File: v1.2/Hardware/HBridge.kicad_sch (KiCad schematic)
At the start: 54 parts, among them J10 DG25C-B-04P-13-00AH, J3 Screw_Terminal_01x03, J9 DG25C-B-04P-13-00AH, Q1 IXGH48N60C3D1, Q2 IXGH48N60C3D1, Q23 BC817, Q24 BC817, U8 HCPL-3120, U9 HCPL-3120

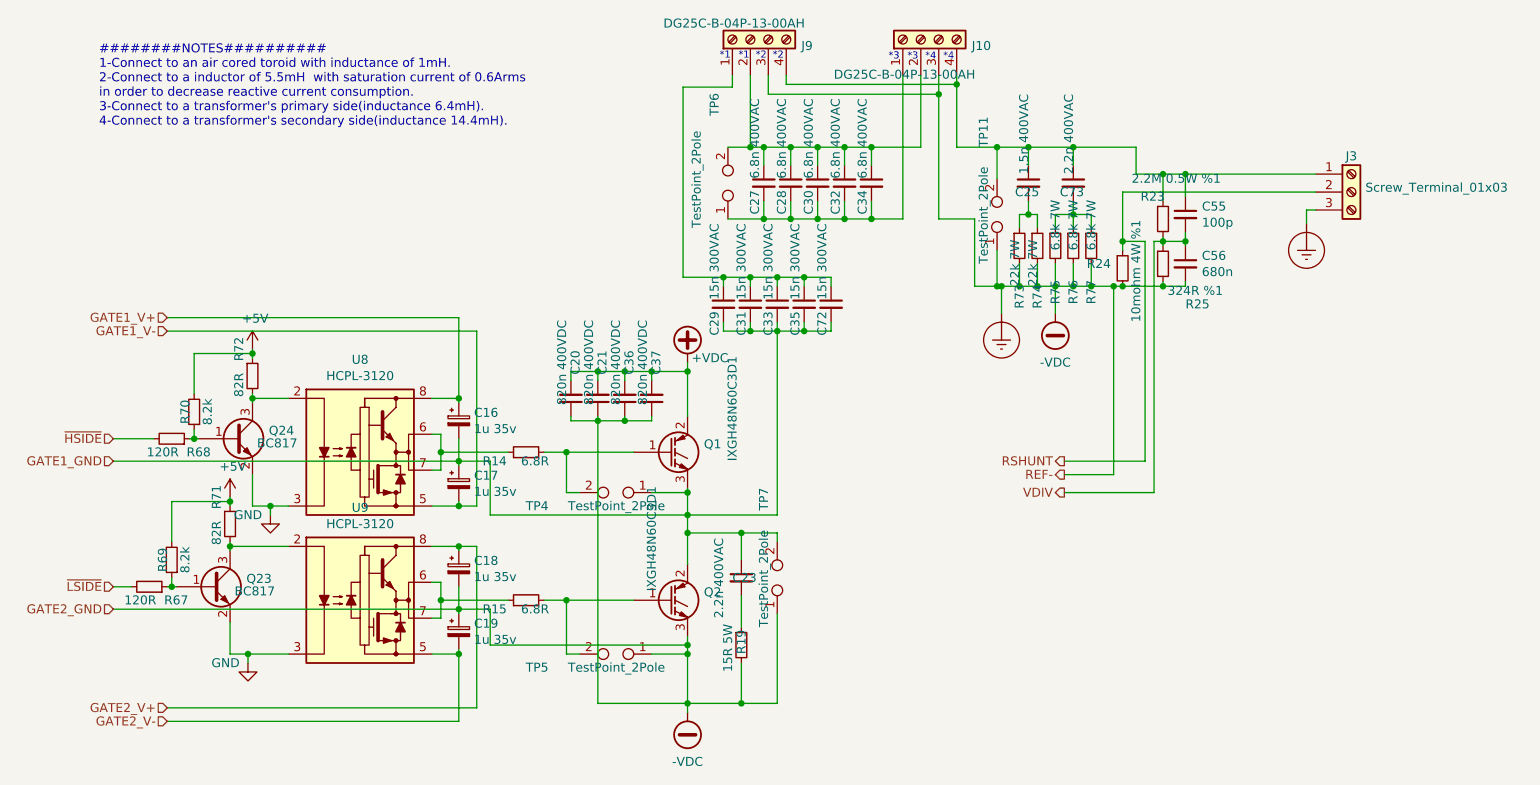
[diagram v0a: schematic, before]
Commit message: Addition of firmware to v1.2(not tested)
+Addition of power tracking(with duty cycle control).
+Addition of resonance freq tracking(via proprietary algorithm relied on active and reactive power measurements)
+Quality factor monitoring
+Power boost when loaded(idle and loaded modes)
+Much better frequency resolution(less than 1Hz)
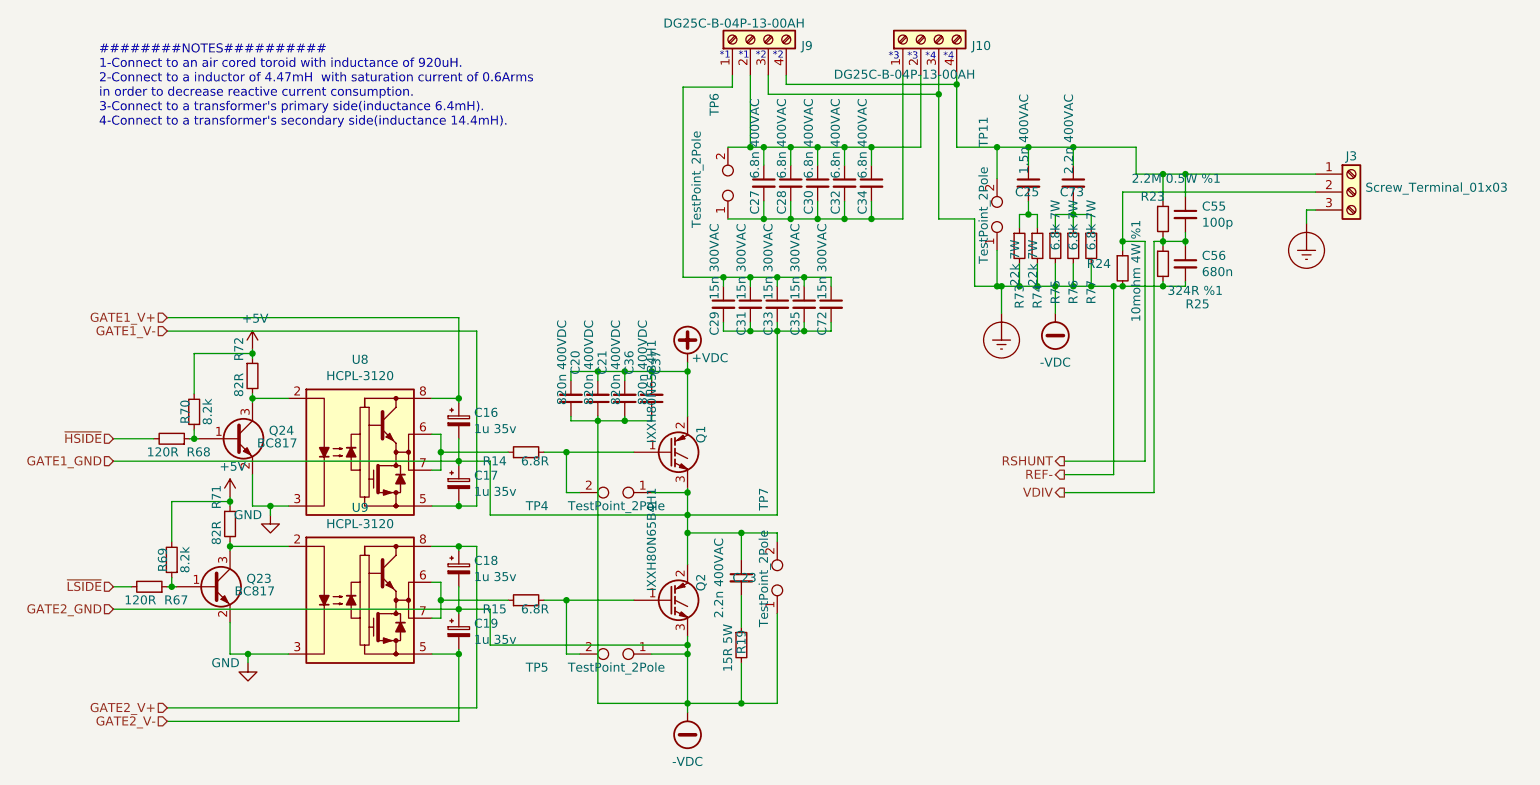
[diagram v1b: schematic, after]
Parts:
- Q1, Q2: value IXGH48N60C3D1 -> IXXH80N65B4H1; Link https://www.ozdisan.com/power-semiconductors/igbts/discrete-igbts/IXGH48N60C3D1 -> https://www.ozdisan.com/power-semiconductors/igbts/discrete-igbts/IXXH80N65B4H1; Price 25.41445TL -> 31.80527TL
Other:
- note added: "########NOTES########## 1-Connect to an air cored toroid with inductance of 920uH. 2-Connect to a inductor of 4.47mH with saturation current of 0.6Arms in order to decrease reactive current consumption. 3-Connect to a transformer's primary side(inductance 6.4mH). 4-Connect to a transformer's secondary side(inductance 14.4mH)."
- note removed: "########NOTES########## 1-Connect to an air cored toroid with inductance of 1mH. 2-Connect to a inductor of 5.5mH with saturation current of 0.6Arms in order to decrease reactive current consumption. 3-Connect to a transformer's primary side(inductance 6.4mH). 4-Connect to a transformer's secondary side(inductance 14.4mH)."

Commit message: Start of rs485 communication interface development.
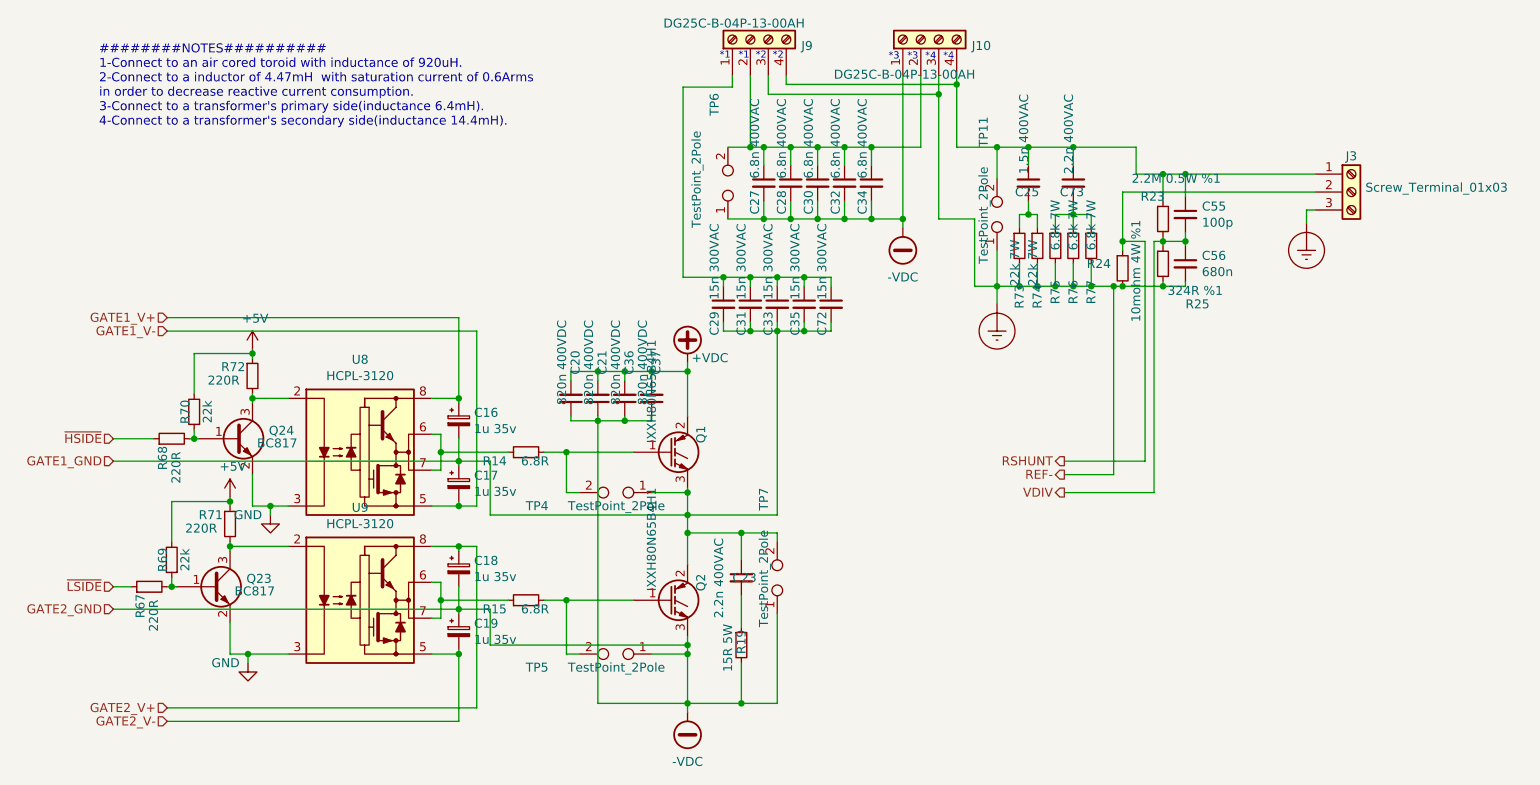
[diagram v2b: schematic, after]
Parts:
- R67, R68: value 120R -> 220R; Link https://ozdisan.com/passive-components/resistors/smt-smd-and-chip-resistors/0805S8J0121T5E -> https://ozdisan.com/passive-components/resistors/smt-smd-and-chip-resistors/0805S8J0221T5E; Price 0.01492TL -> 0.01498TL
- R69, R70: value 8.2k -> 22k; Link https://ozdisan.com/passive-components/resistors/smt-smd-and-chip-resistors/0805S8J0822T5E -> https://ozdisan.com/passive-components/resistors/smt-smd-and-chip-resistors/0805S8J0223TDE; Price 0.01518TL -> 0.01877TL
- R71, R72: value 82R -> 220R; Link https://ozdisan.com/passive-components/resistors/smt-smd-and-chip-resistors/0805S8J0820T5E -> https://ozdisan.com/passive-components/resistors/smt-smd-and-chip-resistors/0805S8J0221T5E; Price 0.01518TL -> 0.01498TL
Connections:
- net -VDC: now also C27.2, C28.2, C30.2, C32.2, C34.2, J10.1 (Pin_1), TP6.1; no longer C56.2, J10.3 (Pin_3), J3.3 (Pin_3), J9.3 (Pin_3), R24.2, R25.2, R73.2, R74.2, R75.2, R76.2, R77.2, TP11.1
- net ~HSIDE: now also R68.1; no longer R68.2
- net ~LSIDE: now also R67.1; no longer R67.2
- net at Q24.1 (B), R70.1: now also R68.2; no longer R68.1
- net at Q23.1 (B), R69.1: now also R67.2; no longer R67.1
- new net Earth_Protective: C56.2, J10.3 (Pin_3), J3.3 (Pin_3), J9.3 (Pin_3), R24.2, R25.2, R73.2, R74.2, R75.2, R76.2, R77.2, TP11.1

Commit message: Redesign.
+Cli interface.
+Modularity improvement(complex number and pid modules created)
+Range change.
+Core-Lattice seperated. 
+Improvement of the control function
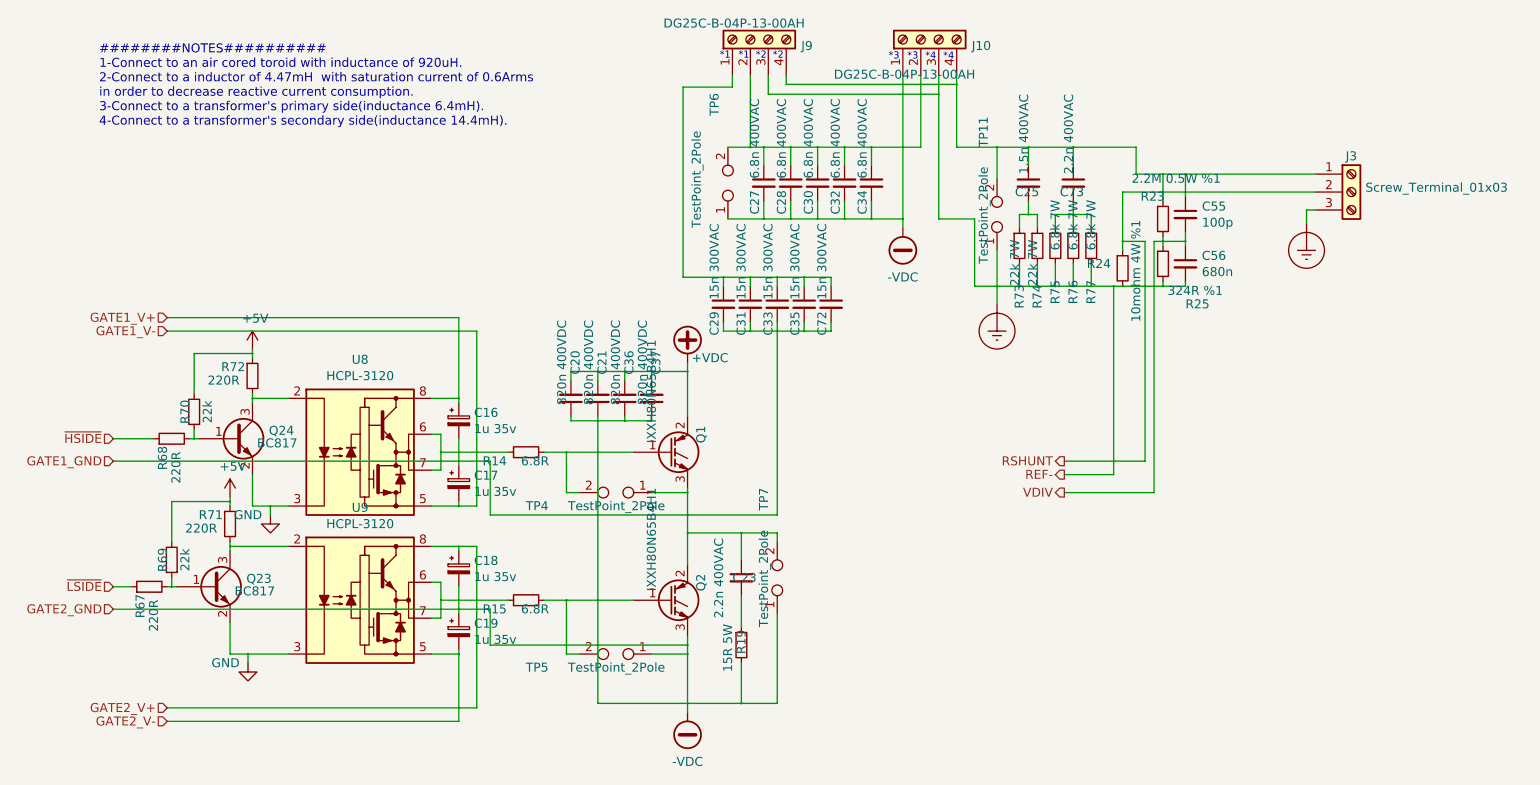
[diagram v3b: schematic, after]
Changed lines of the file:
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@@
-(kicad_sch (version 20200618) (host eeschema "5.99.0-unknown-f3f1740~101~ubuntu18.04.1")
+(kicad_sch (version 20200828) (generator eeschema)
   (page 6 8)
   (paper "A4")
-  (junction (at 59.055 101.6) (diameter 0) (color 0 0 0 0))
-  (junction (at 62.23 80.645) (diameter 0) (color 0 0 0 0))
-  (junction (at 67.31 89.535) (diameter 0) (color 0 0 0 0))
-  (junction (at 67.31 95.885) (diameter 0) (color 0 0 0 0))
-  (junction (at 69.85 111.125) (diameter 0) (color 0 0 0 0))
-  (junction (at 70.485 68.58) (diameter 0) (color 0 0 0 0))
-  (junction (at 70.485 74.93) (diameter 0) (color 0 0 0 0))
-  (junction (at 73.025 90.17) (diameter 0) (color 0 0 0 0))
-  (junction (at 97.155 82.55) (diameter 0) (color 0 0 0 0))
-  (junction (at 97.155 103.505) (diameter 0) (color 0 0 0 0))
-  (junction (at 99.695 74.93) (diameter 0) (color 0 0 0 0))
-  (junction (at 99.695 83.82) (diameter 0) (color 0 0 0 0))
-  (junction (at 99.695 90.17) (diameter 0) (color 0 0 0 0))
-  (junction (at 99.695 95.885) (diameter 0) (color 0 0 0 0))
-  (junction (at 99.695 104.775) (diameter 0) (color 0 0 0 0))
-  (junction (at 99.695 111.125) (diameter 0) (color 0 0 0 0))
-  (junction (at 114.935 82.55) (diameter 0) (color 0 0 0 0))
-  (junction (at 114.935 103.505) (diameter 0) (color 0 0 0 0))
-  (junction (at 119.38 71.12) (diameter 0) (color 0 0 0 0))
-  (junction (at 119.38 78.105) (diameter 0) (color 0 0 0 0))
-  (junction (at 123.19 71.12) (diameter 0) (color 0 0 0 0))
-  (junction (at 123.19 78.105) (diameter 0) (color 0 0 0 0))
-  (junction (at 127 71.12) (diameter 0) (color 0 0 0 0))
-  (junction (at 132.08 71.12) (diameter 0) (color 0 0 0 0))
-  (junction (at 132.08 88.265) (diameter 0) (color 0 0 0 0))
-  (junction (at 132.08 91.44) (diameter 0) (color 0 0 0 0))
-  (junction (at 132.08 93.98) (diameter 0) (color 0 0 0 0))
-  (junction (at 132.08 109.855) (diameter 0) (color 0 0 0 0))
-  (junction (at 132.08 111.125) (diameter 0) (color 0 0 0 0))
-  (junction (at 132.08 118.11) (diameter 0) (color 0 0 0 0))
-  (junction (at 137.16 57.785) (diameter 0) (color 0 0 0 0))
-  (junction (at 139.7 93.98) (diameter 0) (color 0 0 0 0))
-  (junction (at 139.7 118.11) (diameter 0) (color 0 0 0 0))
-  (junction (at 140.97 39.37) (diameter 0) (color 0 0 0 0))
-  (junction (at 140.97 57.785) (diameter 0) (color 0 0 0 0))
-  (junction (at 140.97 65.405) (diameter 0) (color 0 0 0 0))
-  (junction (at 142.875 39.37) (diameter 0) (color 0 0 0 0))
-  (junction (at 142.875 49.53) (diameter 0) (color 0 0 0 0))
-  (junction (at 144.78 57.785) (diameter 0) (color 0 0 0 0))
-  (junction (at 144.78 65.405) (diameter 0) (color 0 0 0 0))
-  (junction (at 146.685 39.37) (diameter 0) (color 0 0 0 0))
-  (junction (at 146.685 49.53) (diameter 0) (color 0 0 0 0))
-  (junction (at 148.59 57.785) (diameter 0) (color 0 0 0 0))
-  (junction (at 148.59 65.405) (diameter 0) (color 0 0 0 0))
-  (junction (at 150.495 39.37) (diameter 0) (color 0 0 0 0))
-  (junction (at 150.495 49.53) (diameter 0) (color 0 0 0 0))
-  (junction (at 154.305 39.37) (diameter 0) (color 0 0 0 0))
-  (junction (at 154.305 49.53) (diameter 0) (color 0 0 0 0))
-  (junction (at 158.115 39.37) (diameter 0) (color 0 0 0 0))
-  (junction (at 158.115 49.53) (diameter 0) (color 0 0 0 0))
-  (junction (at 162.56 49.53) (diameter 0) (color 0 0 0 0))
-  (junction (at 167.64 31.877) (diameter 0) (color 0 0 0 0))
-  (junction (at 170.18 30.48) (diameter 0) (color 0 0 0 0))
-  (junction (at 175.895 39.37) (diameter 0) (color 0 0 0 0))
-  (junction (at 175.895 59.055) (diameter 0) (color 0 0 0 0))
-  (junction (at 179.07 59.055) (diameter 0) (color 0 0 0 0))
-  (junction (at 180.34 39.37) (diameter 0) (color 0 0 0 0))
-  (junction (at 180.34 48.895) (diameter 0) (color 0 0 0 0))
-  (junction (at 181.61 59.055) (diameter 0) (color 0 0 0 0))
-  (junction (at 184.15 59.055) (diameter 0) (color 0 0 0 0))
-  (junction (at 186.69 39.37) (diameter 0) (color 0 0 0 0))
-  (junction (at 186.69 48.895) (diameter 0) (color 0 0 0 0))
-  (junction (at 186.69 59.055) (diameter 0) (color 0 0 0 0))
-  (junction (at 189.23 59.055) (diameter 0) (color 0 0 0 0))
-  (junction (at 192.405 59.055) (diameter 0) (color 0 0 0 0))
-  (junction (at 193.675 52.705) (diameter 0) (color 0 0 0 0))
-  (junction (at 193.675 59.055) (diameter 0) (color 0 0 0 0))
-  (junction (at 199.39 43.18) (diameter 0) (color 0 0 0 0))
-  (junction (at 199.39 52.705) (diameter 0) (color 0 0 0 0))
-  (junction (at 199.39 59.055) (diameter 0) (color 0 0 0 0))
-  (junction (at 202.565 43.18) (diameter 0) (color 0 0 0 0))
-  (junction (at 202.565 52.705) (diameter 0) (color 0 0 0 0))
+  (junction (at 59.055 101.6) (diameter 0.3048) (color 0 0 0 0))
+  (junction (at 62.23 80.645) (diameter 0.3048) (color 0 0 0 0))
+  (junction (at 67.31 89.535) (diameter 0.3048) (color 0 0 0 0))
+  (junction (at 67.31 95.885) (diameter 0.3048) (color 0 0 0 0))
+  (junction (at 69.85 111.125) (diameter 0.3048) (color 0 0 0 0))
+  (junction (at 70.485 68.58) (diameter 0.3048) (color 0 0 0 0))
+  (junction (at 70.485 74.93) (diameter 0.3048) (color 0 0 0 0))
+  (junction (at 73.025 90.17) (diameter 0.3048) (color 0 0 0 0))
+  (junction (at 97.155 82.55) (diameter 0.3048) (color 0 0 0 0))
+  (junction (at 97.155 103.505) (diameter 0.3048) (color 0 0 0 0))
+  (junction (at 99.695 74.93) (diameter 0.3048) (color 0 0 0 0))
+  (junction (at 99.695 83.82) (diameter 0.3048) (color 0 0 0 0))
+  (junction (at 99.695 90.17) (diameter 0.3048) (color 0 0 0 0))
+  (junction (at 99.695 95.885) (diameter 0.3048) (color 0 0 0 0))
+  (junction (at 99.695 104.775) (diameter 0.3048) (color 0 0 0 0))
+  (junction (at 99.695 111.125) (diameter 0.3048) (color 0 0 0 0))
+  (junction (at 114.935 82.55) (diameter 0.3048) (color 0 0 0 0))
+  (junction (at 114.935 103.505) (diameter 0.3048) (color 0 0 0 0))
+  (junction (at 119.38 71.12) (diameter 0.3048) (color 0 0 0 0))
+  (junction (at 119.38 78.105) (diameter 0.3048) (color 0 0 0 0))
+  (junction (at 123.19 71.12) (diameter 0.3048) (color 0 0 0 0))
+  (junction (at 123.19 78.105) (diameter 0.3048) (color 0 0 0 0))
+  (junction (at 127 71.12) (diameter 0.3048) (color 0 0 0 0))
+  (junction (at 132.08 71.12) (diameter 0.3048) (color 0 0 0 0))
+  (junction (at 132.08 88.265) (diameter 0.3048) (color 0 0 0 0))
+  (junction (at 132.08 91.44) (diameter 0.3048) (color 0 0 0 0))
+  (junction (at 132.08 93.98) (diameter 0.3048) (color 0 0 0 0))
+  (junction (at 132.08 109.855) (diameter 0.3048) (color 0 0 0 0))
+  (junction (at 132.08 111.125) (diameter 0.3048) (color 0 0 0 0))
+  (junction (at 132.08 118.11) (diameter 0.3048) (color 0 0 0 0))
+  (junction (at 137.16 57.785) (diameter 0.3048) (color 0 0 0 0))
+  (junction (at 139.7 93.98) (diameter 0.3048) (color 0 0 0 0))
+  (junction (at 139.7 118.11) (diameter 0.3048) (color 0 0 0 0))
+  (junction (at 140.97 39.37) (diameter 0.3048) (color 0 0 0 0))
+  (junction (at 140.97 57.785) (diameter 0.3048) (color 0 0 0 0))
+  (junction (at 140.97 65.405) (diameter 0.3048) (color 0 0 0 0))
+  (junction (at 142.875 39.37) (diameter 0.3048) (color 0 0 0 0))
+  (junction (at 142.875 49.53) (diameter 0.3048) (color 0 0 0 0))
+  (junction (at 144.78 57.785) (diameter 0.3048) (color 0 0 0 0))
+  (junction (at 144.78 65.405) (diameter 0.3048) (color 0 0 0 0))
+  (junction (at 146.685 39.37) (diameter 0.3048) (color 0 0 0 0))
+  (junction (at 146.685 49.53) (diameter 0.3048) (color 0 0 0 0))
+  (junction (at 148.59 57.785) (diameter 0.3048) (color 0 0 0 0))
+  (junction (at 148.59 65.405) (diameter 0.3048) (color 0 0 0 0))
+  (junction (at 150.495 39.37) (diameter 0.3048) (color 0 0 0 0))
+  (junction (at 150.495 49.53) (diameter 0.3048) (color 0 0 0 0))
+  (junction (at 154.305 39.37) (diameter 0.3048) (color 0 0 0 0))
+  (junction (at 154.305 49.53) (diameter 0.3048) (color 0 0 0 0))
+  (junction (at 158.115 39.37) (diameter 0.3048) (color 0 0 0 0))
+  (junction (at 158.115 49.53) (diameter 0.3048) (color 0 0 0 0))
+  (junction (at 162.56 49.53) (diameter 0.3048) (color 0 0 0 0))
+  (junction (at 167.64 31.877) (diameter 0.3048) (color 0 0 0 0))
+  (junction (at 170.18 30.48) (diameter 0.3048) (color 0 0 0 0))
+  (junction (at 175.895 39.37) (diameter 0.3048) (color 0 0 0 0))
+  (junction (at 175.895 59.055) (diameter 0.3048) (color 0 0 0 0))
+  (junction (at 179.07 59.055) (diameter 0.3048) (color 0 0 0 0))
+  (junction (at 180.34 39.37) (diameter 0.3048) (color 0 0 0 0))
+  (junction (at 180.34 48.895) (diameter 0.3048) (color 0 0 0 0))
+  (junction (at 181.61 59.055) (diameter 0.3048) (color 0 0 0 0))
+  (junction (at 184.15 59.055) (diameter 0.3048) (color 0 0 0 0))
+  (junction (at 186.69 39.37) (diameter 0.3048) (color 0 0 0 0))
+  (junction (at 186.69 48.895) (diameter 0.3048) (color 0 0 0 0))
+  (junction (at 186.69 59.055) (diameter 0.3048) (color 0 0 0 0))
+  (junction (at 189.23 59.055) (diameter 0.3048) (color 0 0 0 0))
+  (junction (at 192.405 59.055) (diameter 0.3048) (color 0 0 0 0))
+  (junction (at 193.675 52.705) (diameter 0.3048) (color 0 0 0 0))
+  (junction (at 193.675 59.055) (diameter 0.3048) (color 0 0 0 0))
+  (junction (at 199.39 43.18) (diameter 0.3048) (color 0 0 0 0))
+  (junction (at 199.39 52.705) (diameter 0.3048) (color 0 0 0 0))
+  (junction (at 199.39 59.055) (diameter 0.3048) (color 0 0 0 0))
+  (junction (at 202.565 43.18) (diameter 0.3048) (color 0 0 0 0))
+  (junction (at 202.565 52.705) (diameter 0.3048) (color 0 0 0 0))
   (wire (pts (xy 50.8 80.645) (xy 56.515 80.645))
     (stroke (width 0) (type solid) (color 0 0 0 0))
